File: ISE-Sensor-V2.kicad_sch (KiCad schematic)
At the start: 6 parts, among them CN1 BM04B-SRSS-TB(LF)(SN)

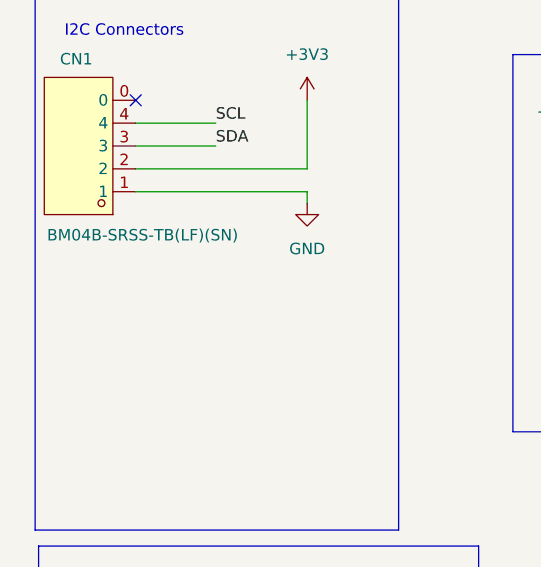
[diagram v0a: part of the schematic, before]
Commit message: Add output images
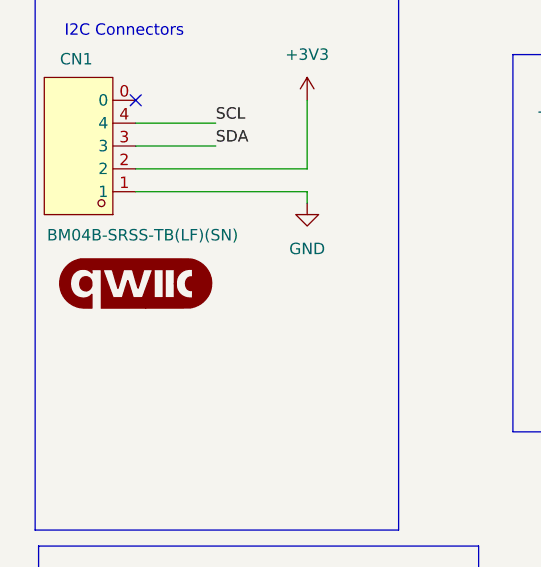
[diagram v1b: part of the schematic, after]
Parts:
- added G1: qwiic_Logo, symbol SparkFun-Qwiic:qwiic_Logo
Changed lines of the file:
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@@
 	(generator "eeschema")
 	(generator_version "9.0")
-	(paper "A1")
+	(paper "A4")
 	(rectangle
 		(start 19.304 20.447)
@@
 					(unit 1)
 				)
+			)
+		)
+	)
+	(symbol
+		(lib_id "SparkFun-Qwiic:qwiic_Logo")
+		(at 30.48 52.07 0)
+		(unit 1)
+		(exclude_from_sim no)
+		(in_bom yes)
+		(on_board no)
+		(dnp no)
+		(fields_autoplaced yes)
+		(property "Reference" "G1"
+			(at 30.48 48.26 0)
+			(effects
+				(font
+					(size 1.27 1.27)
+				)
+				(hide yes)
+			)
+		)
+		(property "Value" "qwiic_Logo"
+			(at 30.48 55.88 0)
+			(effects
+				(font
+					(size 1.27 1.27)
+				)
+				(hide yes)
+			)
+		)
+		(property "Footprint" ""
+			(at 30.48 58.42 0)
+			(effects
+				(font
+					(size 1.27 1.27)
+				)
+				(hide yes)
+			)
+		)
+		(property "Datasheet" ""
+			(at 30.48 52.07 0)
+			(effects
+				(font
+					(size 1.27 1.27)
+				)
+				(hide yes)
+			)
+		)
+		(property "Description" ""
+			(at 30.48 52.07 0)
+			(effects
+				(font
+					(size 1.27 1.27)
+				)
+				(hide yes)
+			)
+		)
+		(instances
+			(project ""
+				(path "/110b63f4-d792-4521-af4c-9d74a08291ce"
+					(reference "G1")
+					(unit 1)
+				)

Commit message: Updates
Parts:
- removed RF3: ORP Sensor, EasyEDA:BNC-TH_DOSIN-801-0051, symbol EasyEDA:DOSIN-801-0050
- added ISE1: DOSIN-801-0080, EasyEDA:BNC-TH_DOSIN-801-0080, symbol EasyEDA:DOSIN-801-0080
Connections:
- net ORP/ISE_GND: now also ISE1.1, ISE1.2, ISE1.3, ISE1.4
- net ORP/ISE_SEN: now also ISE1.5
- net ISO_3V3 renamed PP_ISO_3V3
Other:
- sheet ORP ports: added PP_ISO_3V3; removed ISO_3V3
- note added: "I2C Address"
- note added: "I2C Pullup"
- moved on the sheet: JP3, JP4
